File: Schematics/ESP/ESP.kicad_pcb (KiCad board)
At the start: 2 copper layers, 180.5 x 111.7 mm, 76 parts, among them J1 Barrel_Jack, J11 Bumper 1, J12 Bumper 2, J13 Battery Input, J14 Conn_02x19_Odd_Even, J15 UltraSconic B, J16 Conn_02x19_Odd_Even, J2 IMU, J3 Battery charger, J4 Motor A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

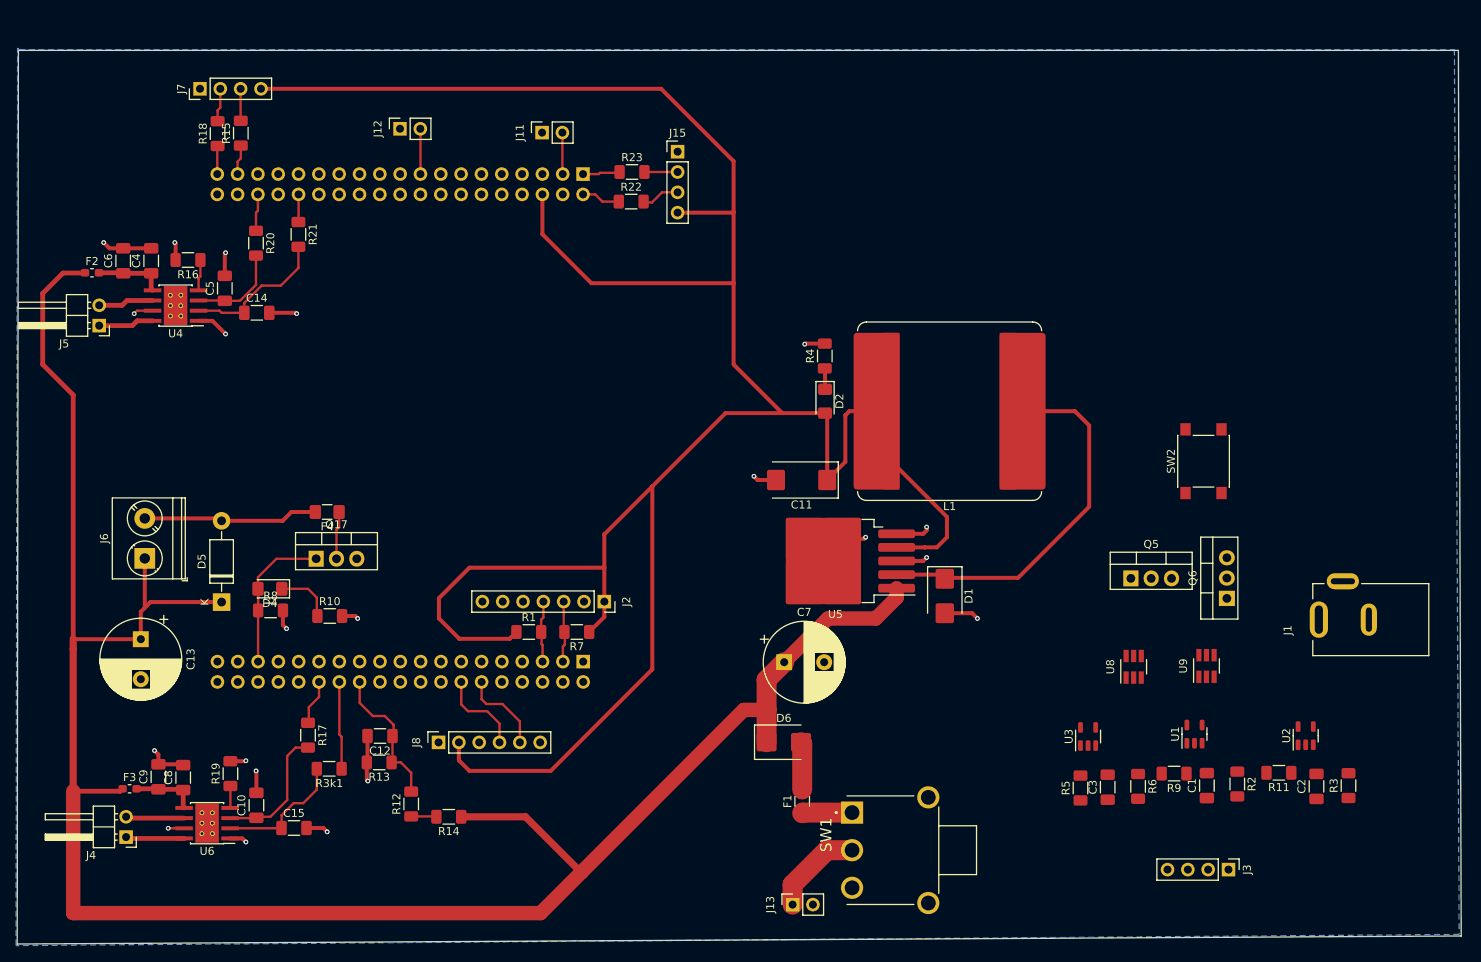
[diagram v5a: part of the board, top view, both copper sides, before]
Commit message: added esp32 connected
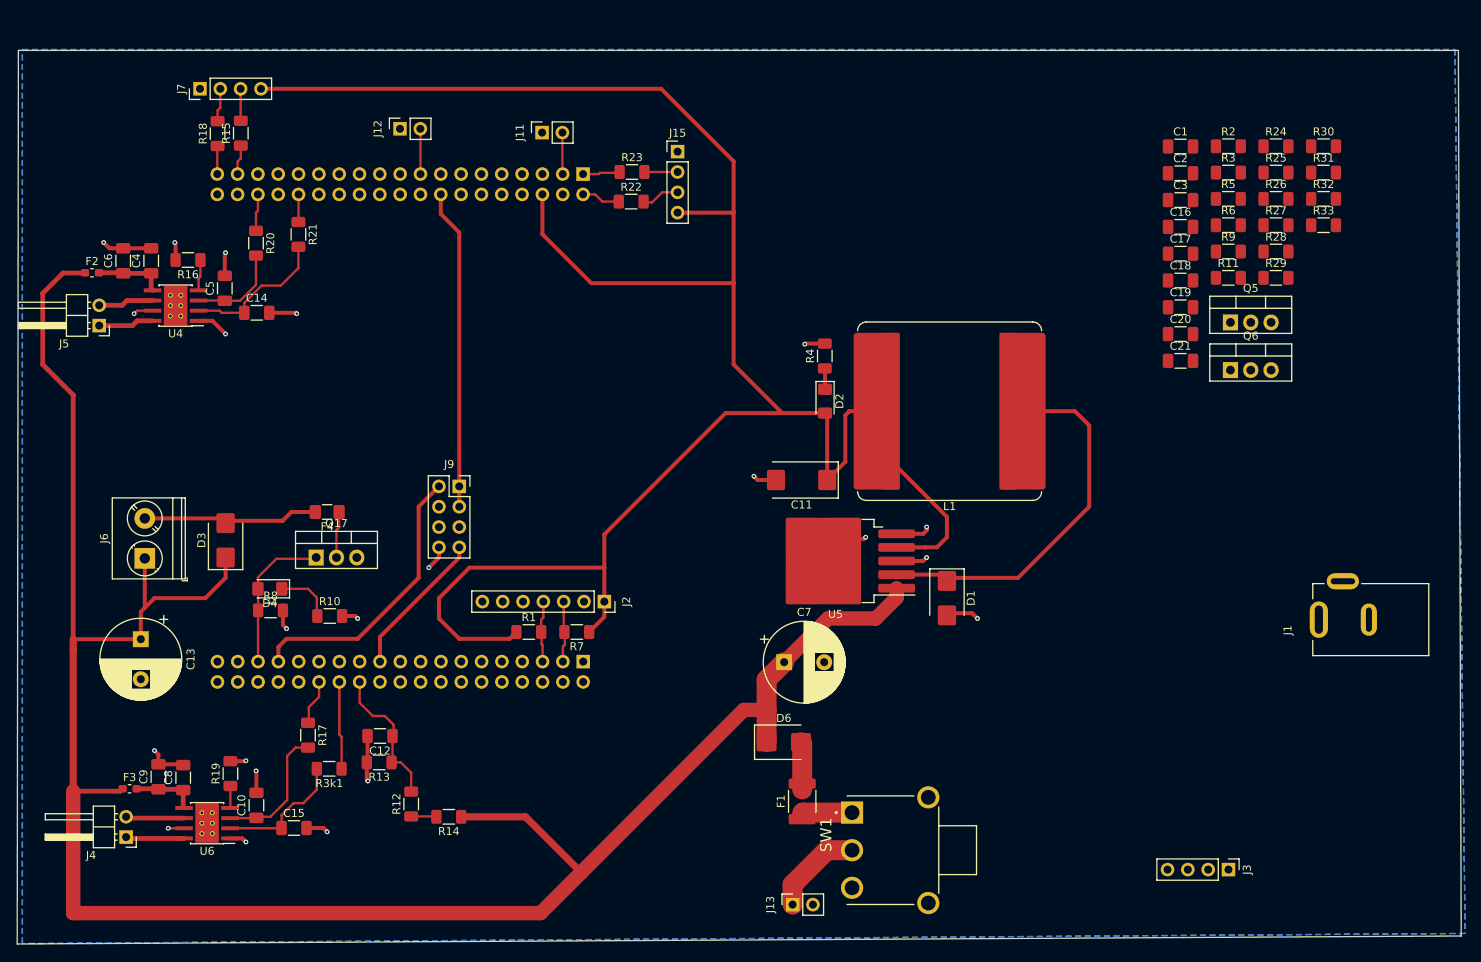
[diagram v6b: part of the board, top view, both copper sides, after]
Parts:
- removed D5: 1N4001, Diode_THT:D_DO-41_SOD81_P10.16mm_Horizontal
- removed J8: BLE, Connector_PinSocket_2.54mm:PinSocket_1x06_P2.54mm_Vertical
- removed SW2: SW_Push, Button_Switch_SMD:SW_SPST_PTS645
- removed U1, U2, U3: AP9101CK, Package_TO_SOT_SMD:SOT-23-5
- removed U8, U9: 74LVC1G11, Package_TO_SOT_SMD:SOT-23-6_Handsoldering
- added C16: 100nF, Capacitor_SMD:C_1206_3216Metric_Pad1.33x1.80mm_HandSolder, F.Cu at (195.6, 81.9)
- added C17: 100nF, Capacitor_SMD:C_1206_3216Metric_Pad1.33x1.80mm_HandSolder, F.Cu at (195.6, 85.2)
- added C18: 1µF, Capacitor_SMD:C_1206_3216Metric_Pad1.33x1.80mm_HandSolder, F.Cu at (195.6, 88.6)
- added C19: 100nF, Capacitor_SMD:C_1206_3216Metric_Pad1.33x1.80mm_HandSolder, F.Cu at (195.6, 91.9)
- added C20: 1µF, Capacitor_SMD:C_1206_3216Metric_Pad1.33x1.80mm_HandSolder, F.Cu at (195.6, 95.3)
- added C21: 1µF, Capacitor_SMD:C_1206_3216Metric_Pad1.33x1.80mm_HandSolder, F.Cu at (195.6, 98.6)
- added D3: PMEG045V050EPDZ, Diode_SMD:D_SMB, F.Cu at (76.2, 121.0)
- added J9: ESP, Connector_PinSocket_2.54mm:PinSocket_2x04_P2.54mm_Vertical, F.Cu at (105.4, 114.3)
- added R24: 450K, Resistor_SMD:R_1206_3216Metric_Pad1.30x1.75mm_HandSolder, F.Cu at (207.5, 71.8)
- added R25: 1M, Resistor_SMD:R_1206_3216Metric_Pad1.30x1.75mm_HandSolder, F.Cu at (207.5, 75.1)
- added R26: 100, Resistor_SMD:R_1206_3216Metric_Pad1.30x1.75mm_HandSolder, F.Cu at (207.5, 78.4)
- added R27: 100, Resistor_SMD:R_1206_3216Metric_Pad1.30x1.75mm_HandSolder, F.Cu at (207.5, 81.7)
- added R28: 100K, Resistor_SMD:R_1206_3216Metric_Pad1.30x1.75mm_HandSolder, F.Cu at (207.5, 84.9)
- added R29: 10K, Resistor_SMD:R_1206_3216Metric_Pad1.30x1.75mm_HandSolder, F.Cu at (207.5, 88.2)
- added R30: 3.3M, Resistor_SMD:R_1206_3216Metric_Pad1.30x1.75mm_HandSolder, F.Cu at (213.4, 71.8)
- added R31: 1k, Resistor_SMD:R_1206_3216Metric_Pad1.30x1.75mm_HandSolder, F.Cu at (213.4, 75.1)
- added R32: 4.5K, Resistor_SMD:R_1206_3216Metric_Pad1.30x1.75mm_HandSolder, F.Cu at (213.4, 78.4)
- added R33: 1M, Resistor_SMD:R_1206_3216Metric_Pad1.30x1.75mm_HandSolder, F.Cu at (213.4, 81.7)
- C1: value 100nF -> 1µF
- D1: value SK42BL-TP -> PMEG045V050EPDZ
- F1: footprint Fuse:Fuse_1206_3216Metric_Pad1.42x1.75mm_HandSolder -> Fuse:Fuse_1812_4532Metric_Pad1.30x3.40mm_HandSolder
- F4: value 0.57A -> 0.72A
- R11, R5, R9: value 2.7k -> 1k
- R17, R20, R21, R3k1: value 3k3 -> 3.3
- R2, R6: value 330 -> 1k
- R3: value 330 -> 10k
- moved C1 80.0 mm to (195.6, 71.8), turned to 0 degrees
- moved R2 79.7 mm to (201.5, 71.8), turned to 0 degrees
- moved C2 78.5 mm to (195.6, 75.2), turned to 0 degrees
- moved R3 78.1 mm to (201.5, 75.1), turned to 0 degrees
- moved R5 75.9 mm to (201.5, 78.4), turned to 0 degrees
- moved C3 74.0 mm to (195.6, 78.5), turned to 0 degrees
- moved R6 71.1 mm to (201.5, 81.7), turned to 0 degrees
- moved R9 65.6 mm to (201.5, 84.9), turned to 0 degrees
- moved R11 62.2 mm to (201.5, 88.2), turned to 0 degrees
- moved Q5 34.3 mm to (201.8, 93.8)
- moved Q6 28.5 mm to (201.8, 99.8), turned to 0 degrees
- moved D1 0.38 mm to (166.4, 128.3)
- moved Q17 0.16 mm to (87.5, 123.2)
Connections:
- C1 pad 1: Cell1+ -> Net-(U1-VDD)
- C1 pad 2: Net-(U1-VDD) -> Cell1-
- C2 pad 1: Cell2+ -> Net-(U1-VC3)
- C2 pad 2: Net-(U2-VDD) -> Net-(U1-VC2)
- C3 pad 1: Battery- -> Net-(U1-VC2)
- C3 pad 2: Net-(U3-VDD) -> Net-(U1-VC1)
- J11 pad 1: Battery- -> Cell1-
- J12 pad 1: Battery- -> Cell1-
- J14 pad 16: unconnected-(J14-Pin_16-Pad16) -> +3.3V
- J14 pad 19: Battery- -> Cell1-
- J14 pad 20: Battery- -> Cell1-
- J14 pad 22: Battery- -> Cell1-
- J14 pad 8: Battery- -> Cell1-
- J15 pad 1: Battery- -> Cell1-
- J16 pad 12: Net-(J16-Pin_12) -> unconnected-(J16-Pin_12-Pad12)
- J16 pad 14: Net-(J16-Pin_14) -> unconnected-(J16-Pin_14-Pad14)
- J16 pad 20: Battery- -> Cell1-
- J16 pad 21: unconnected-(J16-Pin_21-Pad21) -> TX
- J16 pad 31: unconnected-(J16-Pin_31-Pad31) -> RX
- J16 pad 9: Battery- -> Cell1-
- J2 pad 2: Battery- -> Cell1-
- J3 pad 1: Battery+ -> Cell3+
- J3 pad 4: Battery- -> Cell1-
- J7 pad 1: Battery- -> Cell1-
- Q6 pad 3: Battery- -> Net-(Q6-S)
- R11 pad 1: Cell2+ -> Net-(U1-VDD)
- R11 pad 2: Net-(U2-VM) -> Cell3+
- R2 pad 1: Net-(U1-VDD) -> Cell3+
- R2 pad 2: Cell2+ -> Net-(U1-VC3)
- R3 pad 1: Battery+ -> Net-(U1-TS)
- R3 pad 2: Net-(U2-VDD) -> Cell1-
- R5 pad 1: Battery- -> Cell2+
- R5 pad 2: Net-(U3-VM) -> Net-(U1-VC2)
- R6 pad 1: Net-(U3-VDD) -> Cell1+
- R6 pad 2: Cell1+ -> Net-(U1-VC1)
- R9 pad 1: Cell1+ -> Cell1-
- SW1 pad 3: Battery- -> unconnected-(SW1-C-Pad3)
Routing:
- net +5V: track 320.9 -> 265.8 mm
- net +3.3V: track 0.00 -> 40.0 mm
- net RX: track 0.00 -> 35.4 mm
- net TX: track 0.00 -> 18.4 mm
- net Net-(J16-Pin_14): track 10.9 -> 0.00 mm
- net Net-(J16-Pin_12): track 10.7 -> 0.00 mm
- net +12V: track 264.9 -> 269.2 mm
- net Cell1-: track 0.00 -> 3.07 mm, vias 0 -> 1
- added copper zone on B.Cu, net Cell1-
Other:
- board text removed: "Battery Charging circuit"

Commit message: fixed bom
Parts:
- moved J9 15.2 mm to (105.4, 99.1)
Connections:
- C1 pad 2: Cell1- -> Battery-
- C16 pad 2: Cell1- -> Battery-
- C17 pad 2: Cell1- -> Battery-
- C18 pad 1: Cell1- -> Battery-
- C20 pad 2: Cell1- -> Battery-
- C21 pad 2: Cell1- -> Battery-
- J11 pad 1: Cell1- -> Battery-
- J12 pad 1: Cell1- -> Battery-
- J14 pad 19: Cell1- -> Battery-
- J14 pad 20: Cell1- -> Battery-
- J14 pad 22: Cell1- -> Battery-
- J14 pad 8: Cell1- -> Battery-
- J15 pad 1: Cell1- -> Battery-
- J16 pad 20: Cell1- -> Battery-
- J16 pad 9: Cell1- -> Battery-
- J2 pad 2: Cell1- -> Battery-
- J3 pad 4: Cell1- -> Battery-
- J7 pad 1: Cell1- -> Battery-
- J9 pad 8: Cell1- -> Battery-
- R25 pad 2: Cell1- -> Battery-
- R27 pad 2: Cell1- -> Battery-
- R28 pad 2: Cell1- -> Battery-
- R3 pad 2: Cell1- -> Battery-
- R9 pad 1: Cell1- -> Battery-
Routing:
- net +3.3V: track 40.0 -> 24.8 mm
- net TX: track 18.4 -> 33.6 mm
- net RX: track 35.4 -> 50.3 mm
- net Cell1-: track 3.07 -> 0.00 mm, vias 1 -> 0
- removed copper zone on B.Cu, net Cell1-

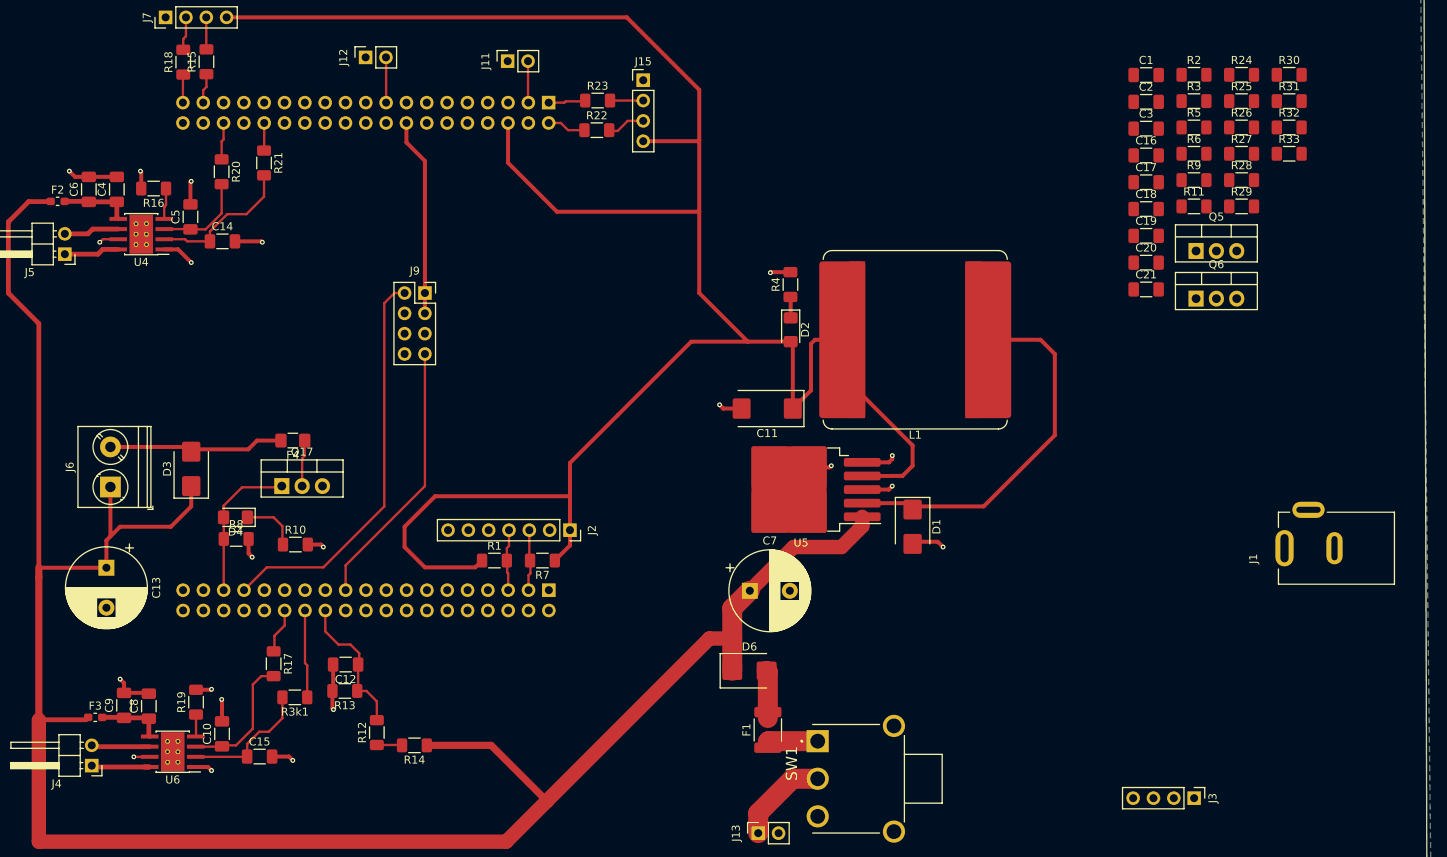
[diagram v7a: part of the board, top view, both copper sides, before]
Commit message: charging IC PCB and cleanup
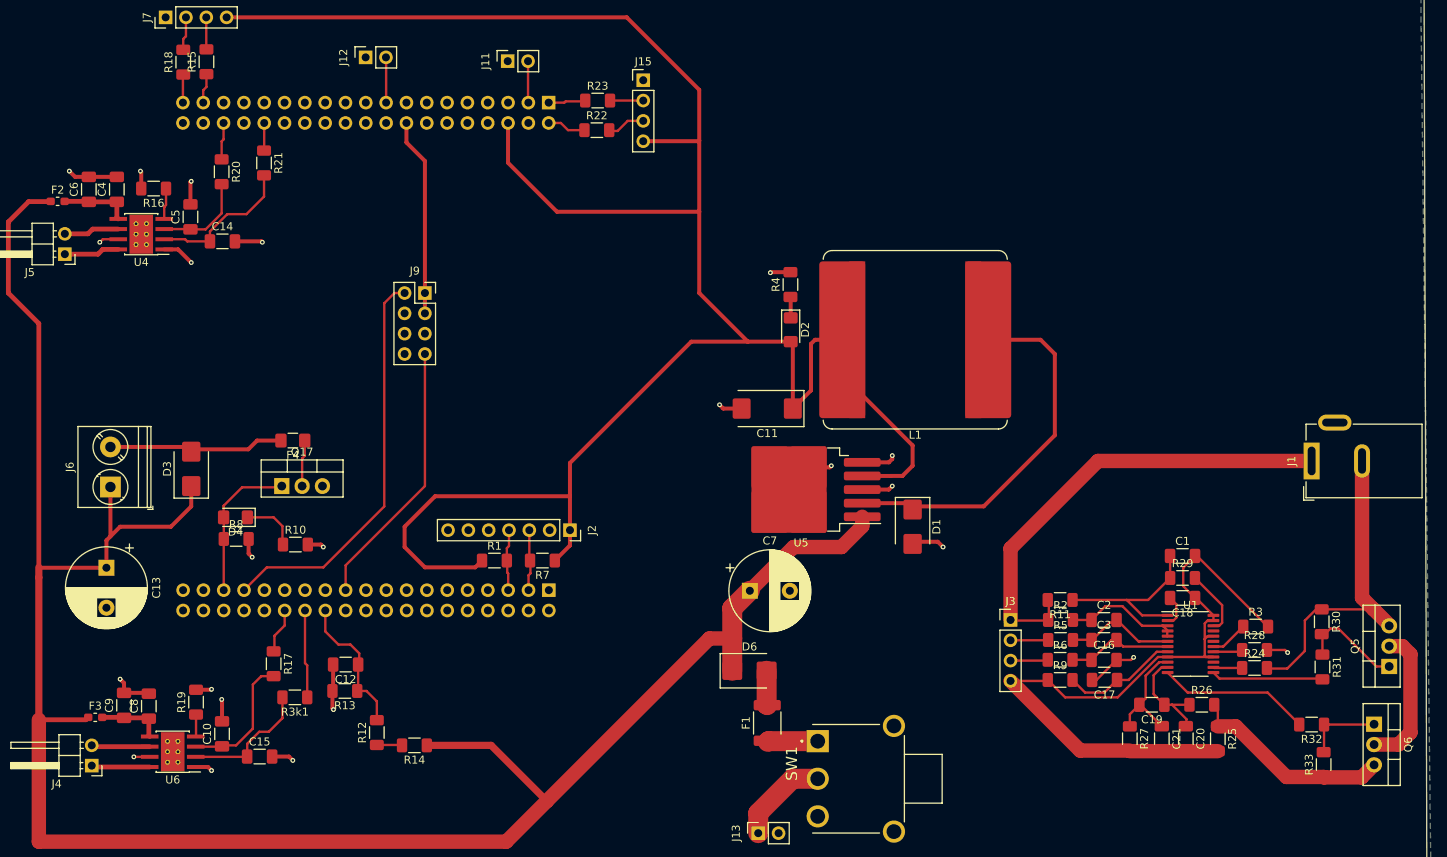
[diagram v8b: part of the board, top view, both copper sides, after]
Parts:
- added U1: BQ7791500PWT, Package_SO:TSSOP-24_4.4x7.8mm_P0.65mm, F.Cu at (201.1, 142.9)
- J1: footprint RAPC722X:SWITCHCRAFT_RAPC722X -> Connector_BarrelJack:BarrelJack_GCT_DCJ200-10-A_Horizontal
- R25: value 1M -> 1m
- moved R25 79.8 mm to (204.5, 154.8), turned to -90 degrees
- moved R33 76.5 mm to (217.8, 158.0), turned to 90 degrees
- moved R32 74.7 mm to (216.2, 153.0), turned to 180 degrees
- moved R27 74.4 mm to (193.5, 154.8), turned to -90 degrees
- moved R24 74.2 mm to (209.1, 145.9)
- moved R26 72.3 mm to (202.5, 150.5)
- moved R31 70.9 mm to (217.6, 145.8), turned to -90 degrees
- moved R2 70.2 mm to (184.9, 139.9)
- moved R30 68.5 mm to (217.5, 140.2), turned to -90 degrees
- moved R5 66.2 mm to (184.9, 142.4)
- moved R3 66.1 mm to (209.2, 140.8)
- moved R6 65.4 mm to (184.8, 144.9)
- moved C2 65.0 mm to (190.3, 139.9)
- moved R9 64.7 mm to (184.8, 147.4)
- moved C3 64.1 mm to (190.3, 142.4)
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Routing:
- net Battery-: track 69.4 -> 166.4 mm, vias 21 -> 23
- net Cell3+: track 0.00 -> 57.5 mm
- net P-: track 0.00 -> 39.7 mm
- net Net-(Q6-S): track 0.00 -> 25.1 mm
- net Net-(U1-VDD): track 0.00 -> 22.0 mm
- net DSG: track 0.00 -> 19.1 mm
- net Net-(Q5-D): track 0.00 -> 18.0 mm
- net Net-(U1-VC3): track 0.00 -> 14.8 mm
- net Net-(U1-VC0): track 0.00 -> 14.7 mm
- net Net-(U1-SRP): track 0.00 -> 14.4 mm
- net CHG: track 0.00 -> 13.8 mm
- net Net-(U1-VC2): track 0.00 -> 13.8 mm
- net Net-(U1-VC1): track 0.00 -> 13.2 mm
- net Net-(Q5-G): track 0.00 -> 13.0 mm
- net Net-(U1-SRN): track 0.00 -> 12.8 mm
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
